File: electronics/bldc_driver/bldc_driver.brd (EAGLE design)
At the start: 50 x 35 mm, 33 parts, among them Q1 MOSFET-N, Q2 MOSFET-N, Q3 MOSFET-N, Q4 MOSFET-N, Q5 MOSFET-N, Q6 MOSFET-N, X1 LOGIC, X2 POWER

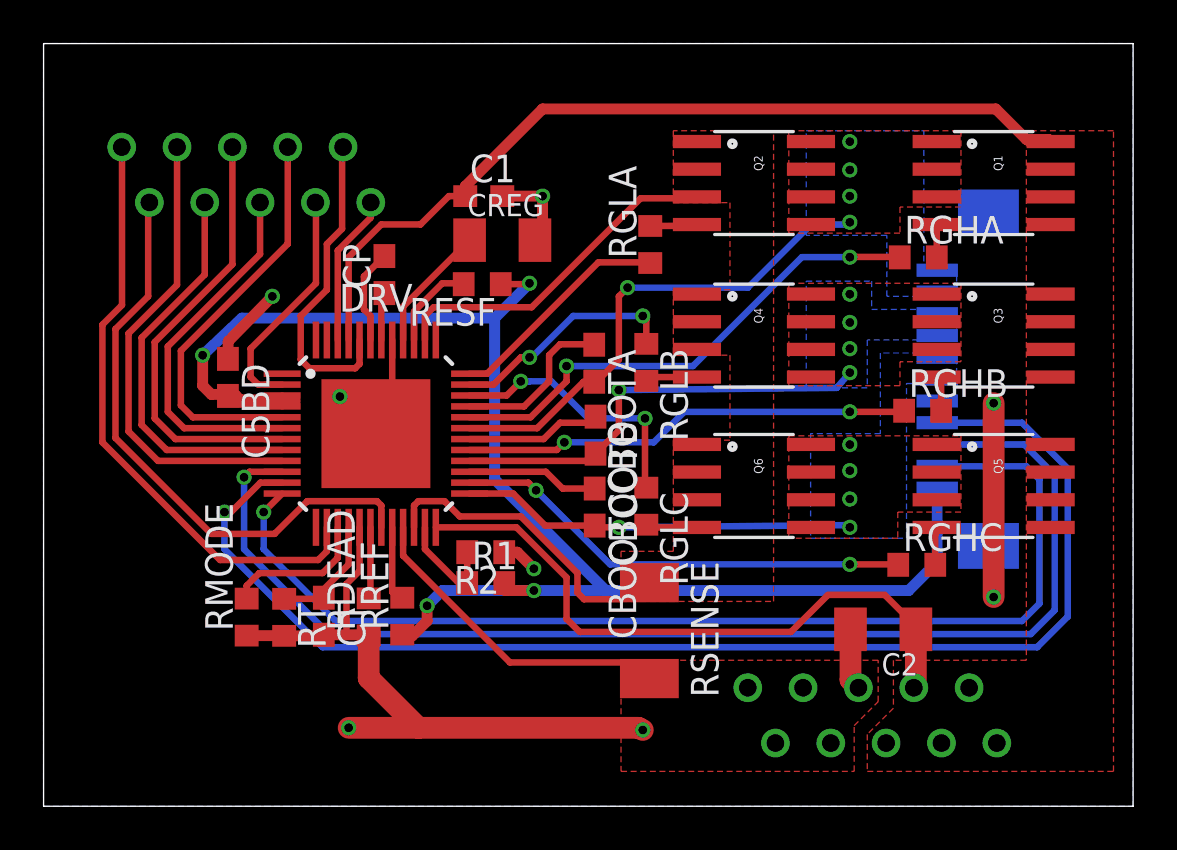
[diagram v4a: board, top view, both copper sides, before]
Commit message: Routed motor driver board
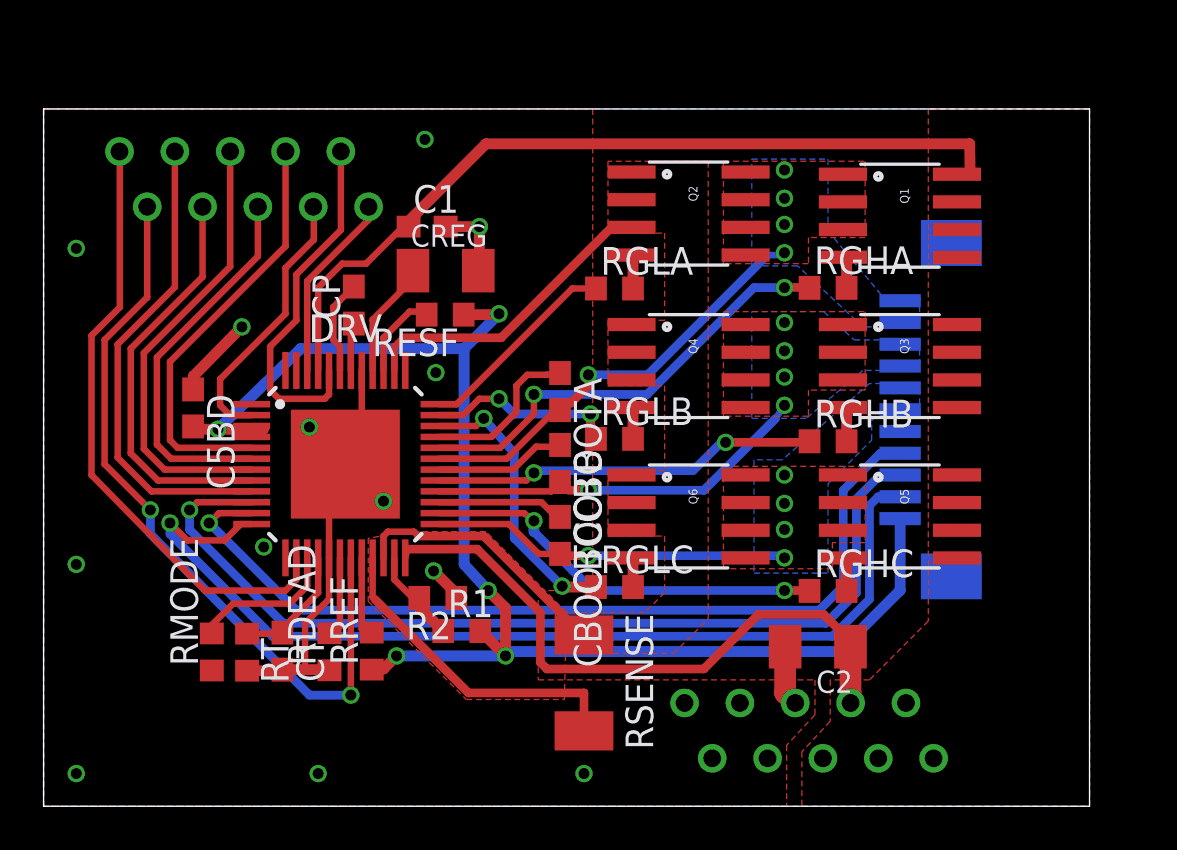
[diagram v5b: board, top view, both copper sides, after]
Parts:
- moved RGHB 4.56 mm to (36.0, 16.8)
- moved Q1 4.55 mm to (39.3, 27.1)
- moved Q3 4.52 mm to (39.3, 20.2)
- moved Q5 4.52 mm to (39.3, 13.3)
- moved RGHA 4.37 mm to (36.0, 23.8)
- moved RGHC 4.24 mm to (36.0, 9.88)
- moved RGLC 3.99 mm to (26.2, 10.1), turned to 0 degrees
- moved RSENSE 3.84 mm to (24.8, 5.66)
- moved RGLB 3.80 mm to (26.2, 16.9), turned to 0 degrees
- moved Q2 3.31 mm to (29.6, 27.2)
- moved Q4 3.31 mm to (29.6, 20.2)
- moved Q6 3.31 mm to (29.6, 13.3)
- moved C2 3.10 mm to (35.5, 7.32)
- moved R2 3.04 mm to (18.1, 9.56)
- moved X2 2.98 mm to (35.1, 3.47)
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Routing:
- net GND: track 73.1 -> 48.2 mm, vias 8 -> 13
- net H2: track 59.7 -> 41.1 mm
- net H1: track 56.6 -> 43.6 mm
- net CSOUT: track 27.2 -> 35.3 mm, vias 0 -> 2
- net H3: track 50.8 -> 45.5 mm
- net +5V: track 71.0 -> 66.8 mm, vias 4 -> 5
- net SA: track 23.2 -> 20.1 mm
- net GHB: track 20.7 -> 17.8 mm
- net GHA: track 23.2 -> 20.6 mm
- net GHC: track 21.2 -> 18.7 mm
- net LSS: track 30.3 -> 27.9 mm
- net SB: track 20.2 -> 17.9 mm
- net GLB: track 10.7 -> 8.74 mm
- net +12V: track 69.1 -> 67.3 mm
- net DIRO: track 14.6 -> 16.3 mm
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- added copper zone on layer 1, net N$13
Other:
- board size 50 x 35 mm -> 48 x 32 mm

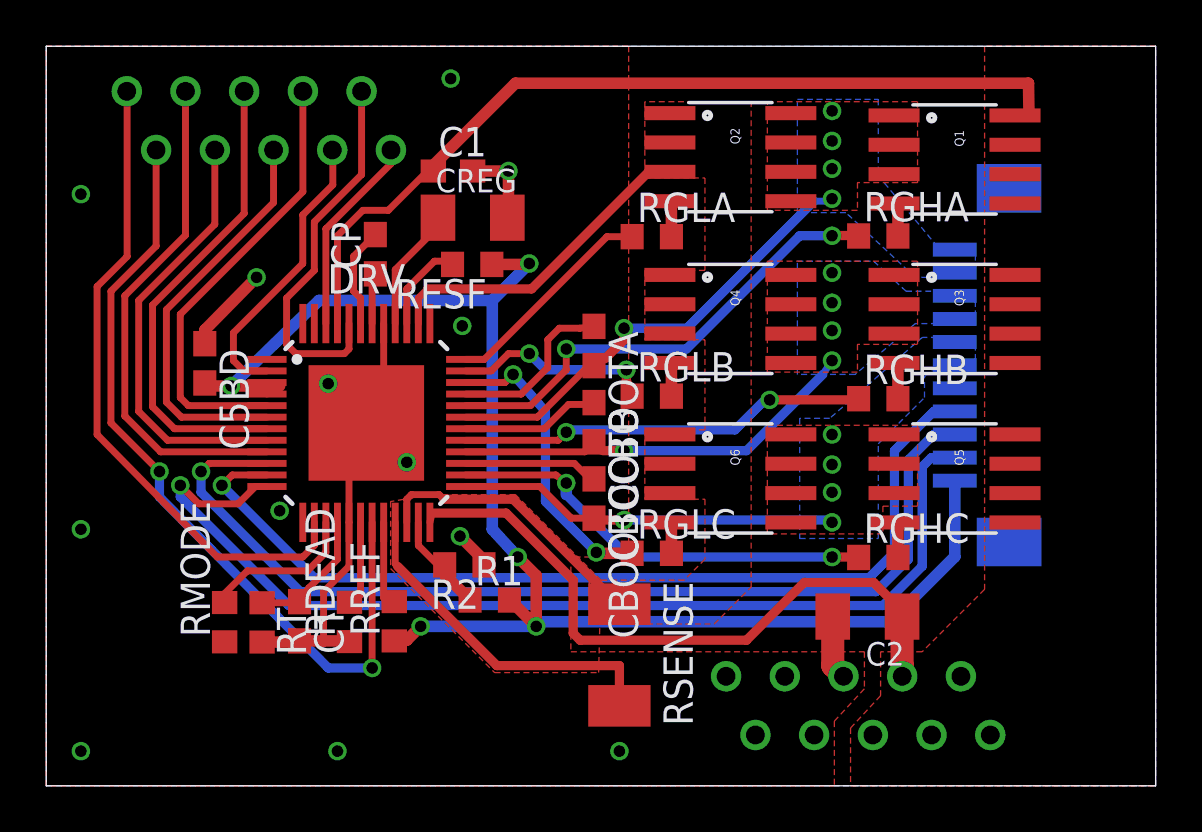
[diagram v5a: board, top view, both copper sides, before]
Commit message: Added pass through transistor for +5V, added +5V and fault LEDs, separated driver and noisy ground with 1 ohm resistor, added 2 GNDs to logic connector, added holes for micro-match connectors
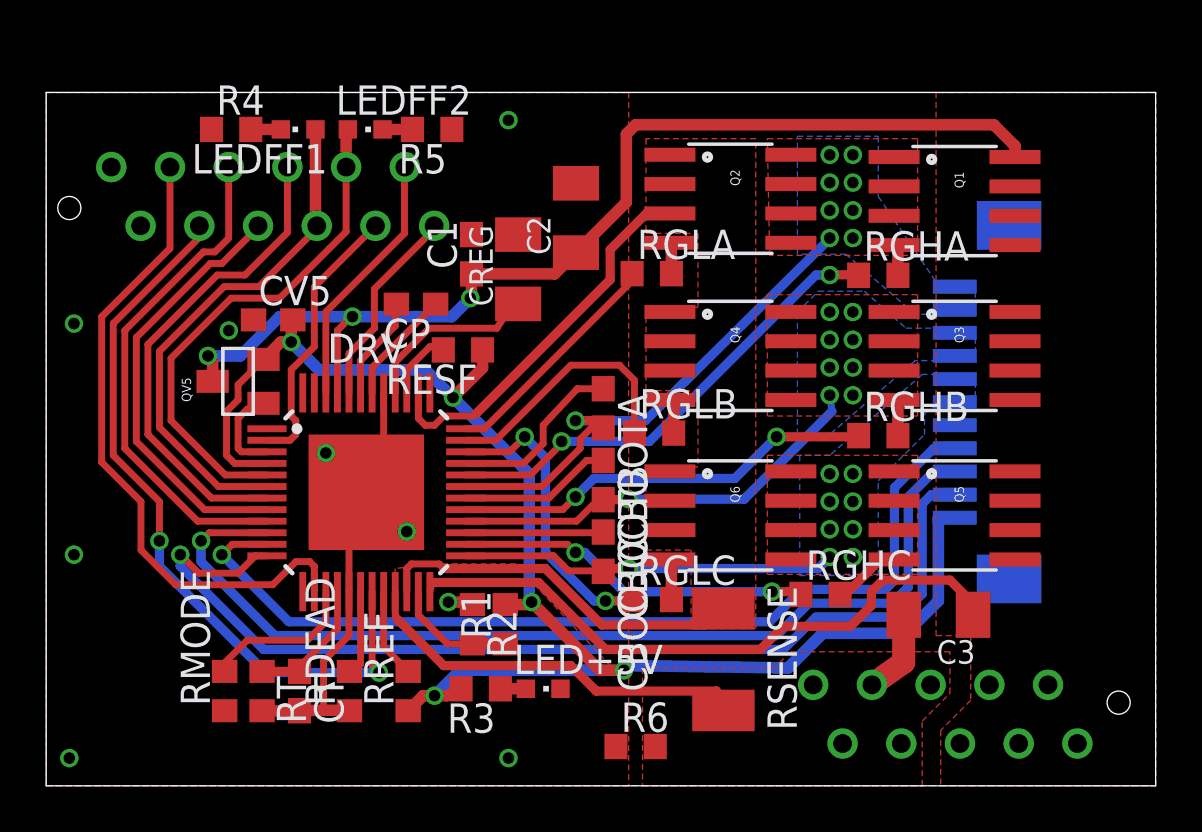
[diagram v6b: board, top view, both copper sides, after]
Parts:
- removed C5BD: 220nF, rcl:C0603
- removed X2: POWER, con-amp-micromatch:MICROMATCH-10
- added C3: 10uF, rcl:C1206K
- added CV5: 220nF, rcl:C0603
- added LED+5V, LEDFF1, LEDFF2: (no value), led:CHIPLED_0603
- added QV5: (no value), SparkFun-DiscreteSemi:SOT23
- added R3, R4, R5: 10k, rcl:R0603
- added R6: 1, rcl:R0603
- added X3: MICROMATCH-10, con-amp-micromatch:MICROMATCH-10
- X1: device con-amp-micromatch:MICROMATCH-10 -> con-amp-micromatch:MICROMATCH-12
- moved C2 21.4 mm to (22.9, 24.6), turned to 90 degrees
- moved RSENSE 4.50 mm to (29.3, 5.46)
- moved RESF 3.72 mm to (18.0, 18.9)
- moved C1 3.69 mm to (18.4, 23.0), turned to 90 degrees
- moved X1 3.33 mm to (9.80, 25.5)
- moved RREF 3.08 mm to (15.7, 4.10)
- moved CT 3.02 mm to (11.0, 4.10)
- moved DRV 3.00 mm to (13.8, 12.7)
- moved RDEAD 2.99 mm to (13.1, 4.10)
- moved RMODE 2.98 mm to (7.72, 4.10)
- moved CREG 2.98 mm to (20.4, 22.4), turned to 90 degrees
- moved RT 2.97 mm to (9.34, 4.10)
- moved RGHC 2.97 mm to (33.5, 8.28)
- moved CP 2.79 mm to (16.0, 20.8), turned to 180 degrees
- moved CBOOTA 2.73 mm to (24.1, 16.3)
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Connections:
- new net GNDA: C3.2, DRV.21, R6.2, RSENSE.2, X3.10, X3.6, X3.7, X3.8, X3.9
- new net N$16: LED+5V.A, R3.1
- new net N$19: LEDFF1.C, R4.2
- new net N$20: LEDFF2.C, R5.2
- new net N$21: DRV.3, QV5.1
- net +12V: now also C3.1, QV5.3, X3.1, X3.2, X3.3, X3.4, X3.5; no longer X2.1, X2.2, X2.3, X2.4, X2.5
- net +5V: now also CV5.2, QV5.2, R3.2; no longer C5BD.2, DRV.3
- net BRAKE: now also X1.6; no longer X1.4
- net COAST: now also X1.11; no longer X1.10
- net CSOUT: now also X1.4; no longer X1.2
- net DIR: now also X1.5; no longer X1.3
- net DIRO: now also X1.12; no longer X1.9
- net FF1: now also LEDFF1.A, X1.8; no longer X1.6
- net FF2: now also LEDFF2.A, X1.9; no longer X1.7
- net GND: now also CV5.1, LED+5V.C, R4.1, R5.1, R6.1, X1.1, X1.2; no longer C5BD.1, DRV.21, RSENSE.2, X2.10, X2.6, X2.7, X2.8, X2.9
- net PWM: now also X1.3; no longer X1.1
- net RESET: now also X1.10; no longer X1.8
- net TACHO: now also X1.7; no longer X1.5
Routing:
- net GND: track 48.2 -> 20.1 mm, vias 13 -> 9
- net GNDA: track 0.00 -> 20.9 mm
- net DIRO: track 16.3 -> 8.73 mm
- net +12V: track 67.3 -> 74.5 mm, vias 0 -> 3
- net LSS: track 27.9 -> 32.9 mm
- net FF1: track 17.4 -> 22.3 mm
- net N$21: track 0.00 -> 3.96 mm
- net GHC: track 18.7 -> 15.4 mm
- net CSOUT: track 35.3 -> 32.1 mm
- net N$8: track 5.35 -> 8.40 mm
- net N$10: track 2.19 -> 5.18 mm
- net SA: track 20.1 -> 22.9 mm, vias 5 -> 9
- net FF2: track 19.3 -> 22.1 mm
- net COAST: track 8.68 -> 11.2 mm
- net GLB: track 8.74 -> 11.2 mm, vias 2 -> 0
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- added copper zone on layer 1, net GNDA
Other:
- board size 48 x 32 mm -> 48 x 30 mm

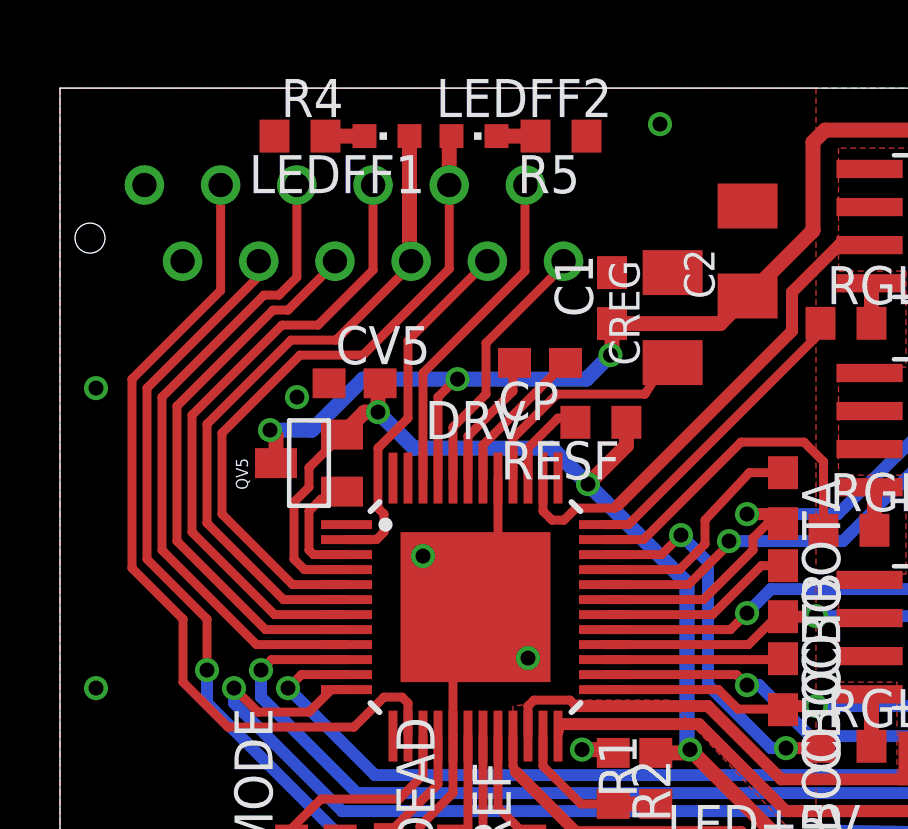
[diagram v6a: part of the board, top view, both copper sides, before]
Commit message: Changed motor driver board logic connector position a bit
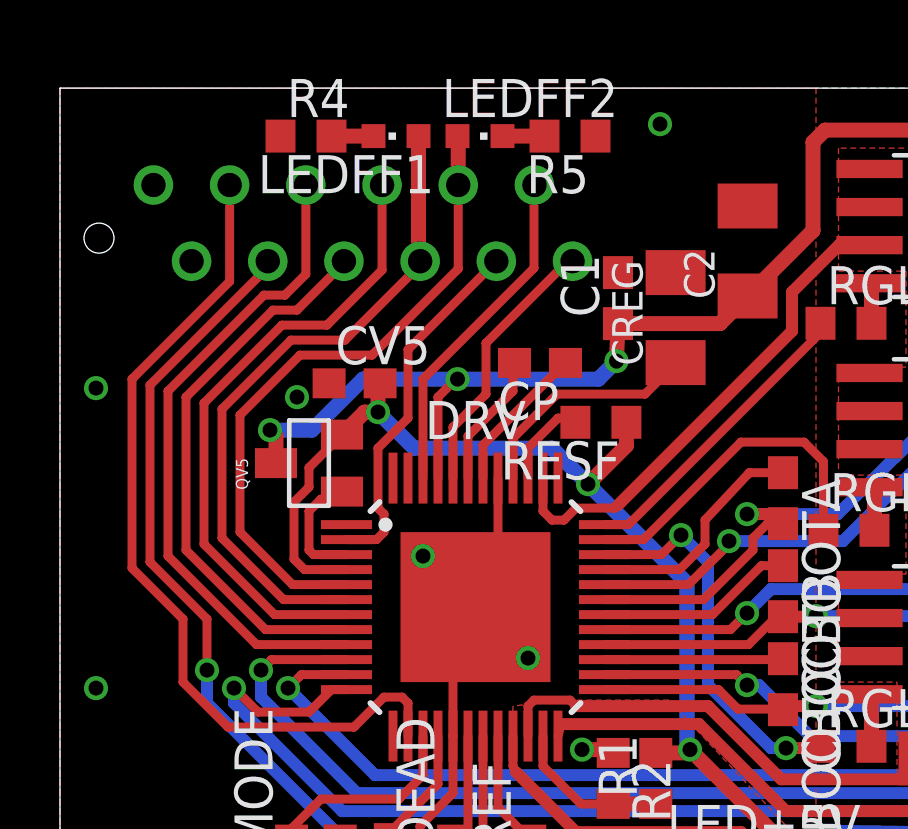
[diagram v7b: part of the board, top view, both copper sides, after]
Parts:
- moved R5 0.30 mm to (17.0, 28.4)
- moved LEDFF1 0.30 mm to (11.2, 28.4)
- moved X1 0.30 mm to (10.1, 25.5)
- moved C1 0.20 mm to (18.6, 23.0)
- moved LEDFF2 0.20 mm to (14.0, 28.4)
- moved R4 0.20 mm to (8.20, 28.4)
- moved CREG 0.10 mm to (20.5, 22.4)
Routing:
- net N$8: track 8.40 -> 7.80 mm

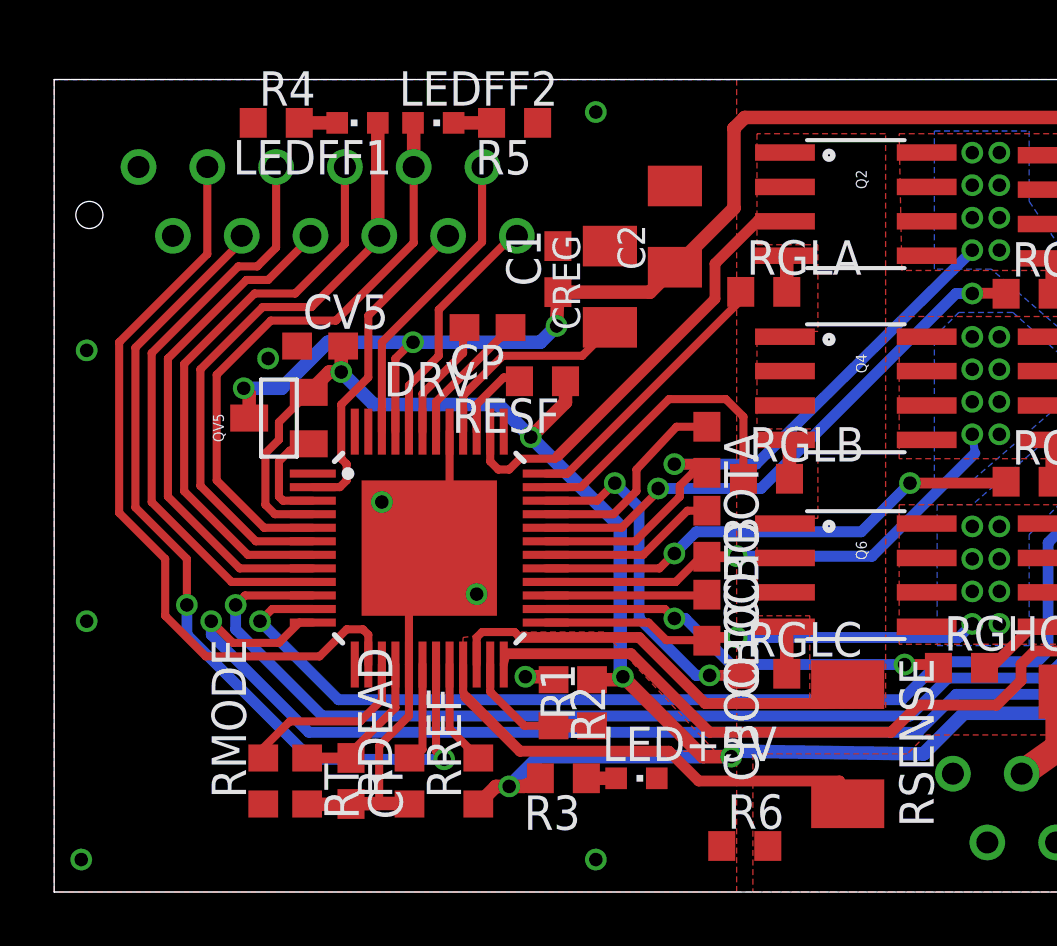
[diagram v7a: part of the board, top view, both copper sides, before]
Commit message: Small motor driver board changes
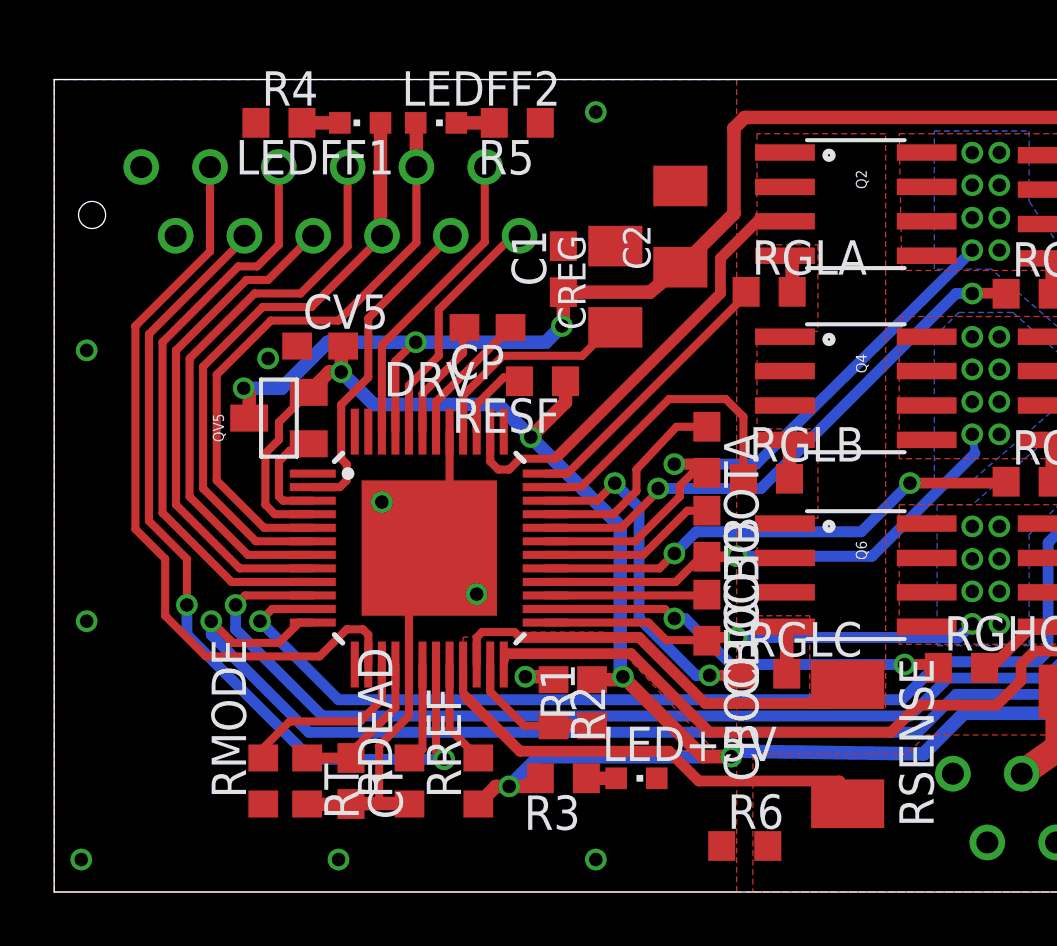
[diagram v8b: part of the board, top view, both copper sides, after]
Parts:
- moved C1 0.20 mm to (18.8, 23.0)
- moved C2 0.20 mm to (23.1, 24.6)
- moved CREG 0.20 mm to (20.7, 22.4)
- moved RGLA 0.20 mm to (26.4, 22.2)
- moved LEDFF1 0.10 mm to (11.3, 28.4)
- moved R4 0.10 mm to (8.30, 28.4)
- moved R5 0.10 mm to (17.1, 28.4)
- moved LEDFF2 0.10 mm to (14.1, 28.4)
- moved X1 0.10 mm to (10.2, 25.5)
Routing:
- net GND: vias 9 -> 10
